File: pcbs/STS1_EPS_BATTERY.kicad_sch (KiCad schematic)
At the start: 10 parts, among them J3 Battery Pack, U13 TMCS1101A3B-Q1, U4 BQ29209DRBT

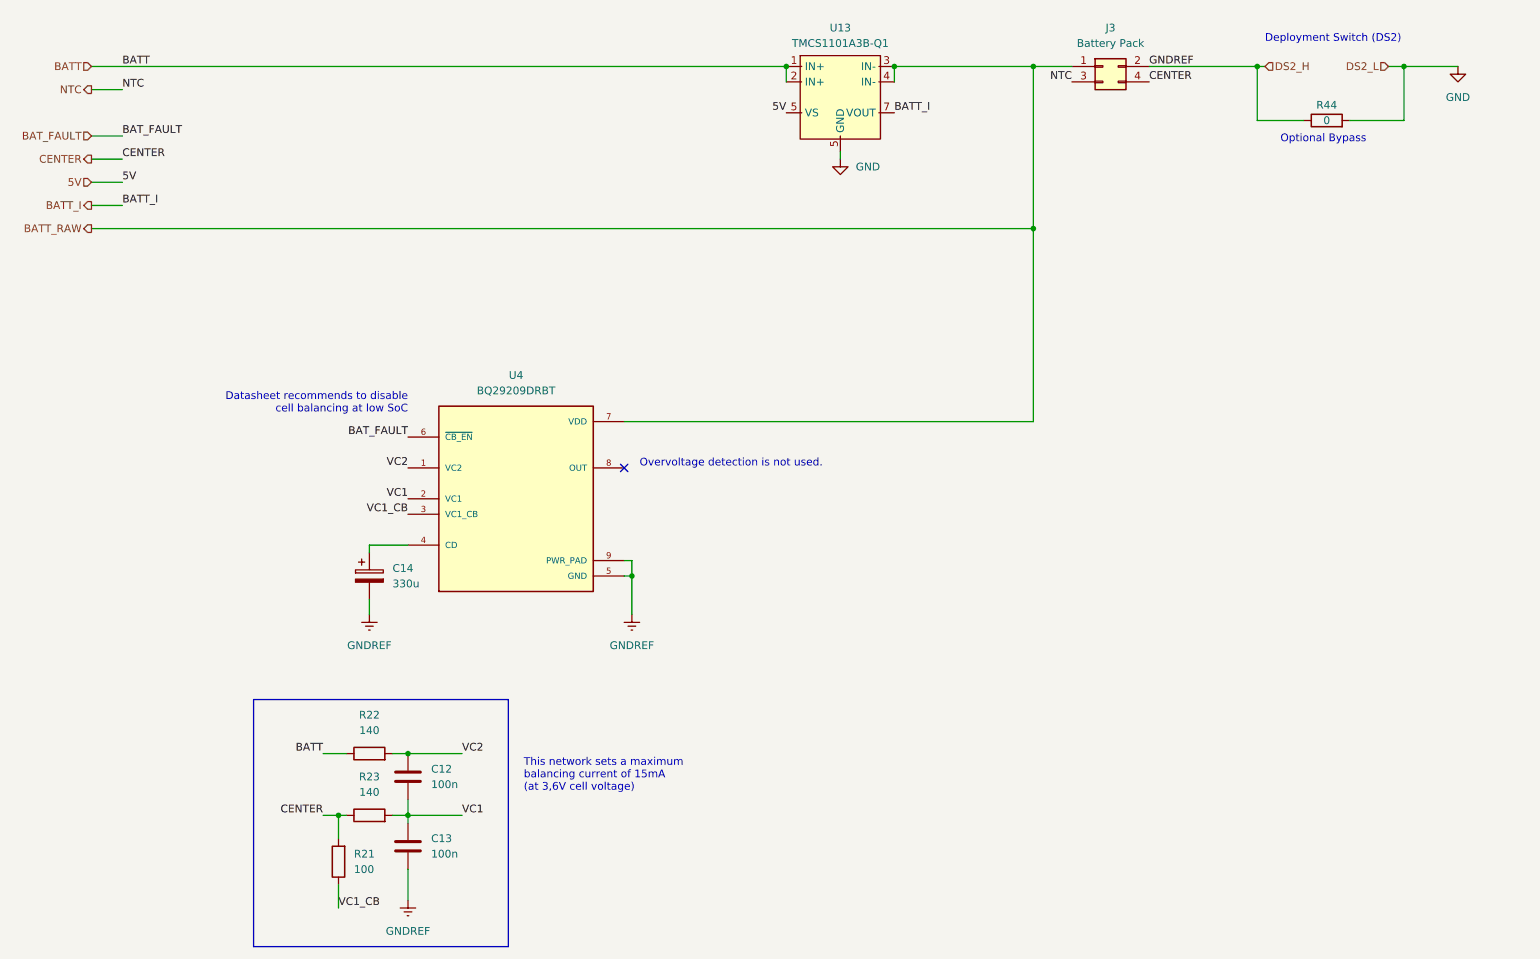
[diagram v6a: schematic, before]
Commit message: Worked on STS1_EPS_2 layout.
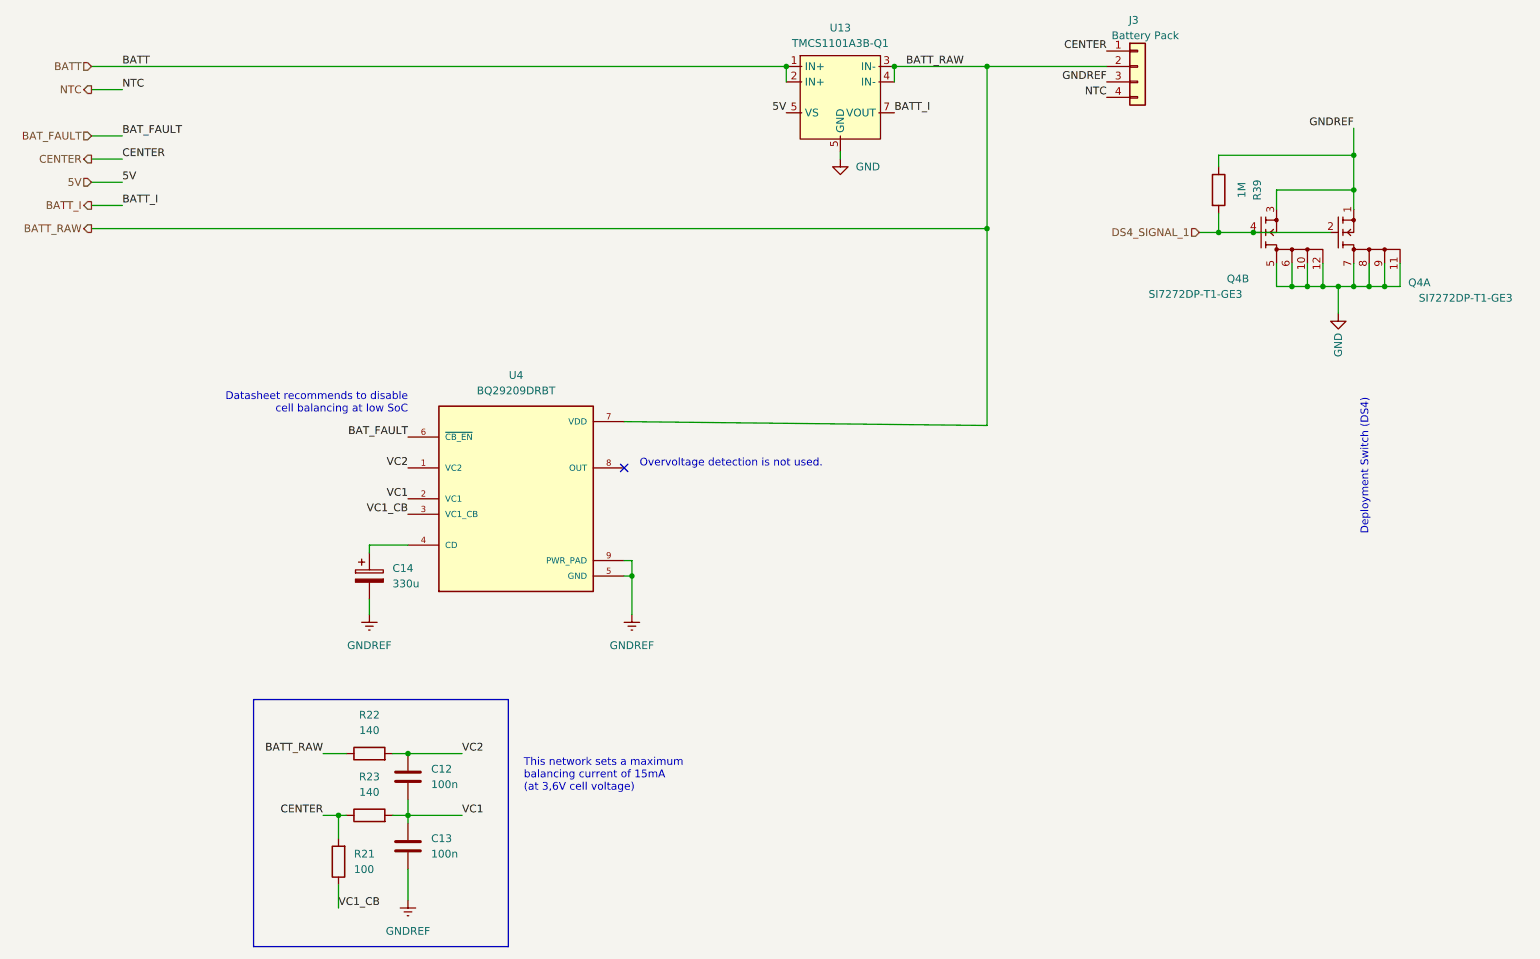
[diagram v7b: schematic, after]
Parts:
- removed R44: 0, Resistor_SMD:R_0805_2012Metric, symbol Device:R
- added Q4: SI7272DP-T1-GE3, STS_Package_SO:POWERPAK_SO8, symbol STS_Transistor_FET:SI7272DP-T1-GE3
- added R39: 1M, Resistor_SMD:R_0805_2012Metric, symbol Device:R
- J3: symbol Connector_Generic:Conn_02x02_Odd_Even -> Connector_Generic:Conn_01x04
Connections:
- net BATT: no longer R22.1
- net BATT_RAW: now also J3.2 (Pin_2), R22.1; no longer J3.1 (Pin_1)
- net CENTER: now also J3.1 (Pin_1); no longer J3.4 (Pin_4)
- net GND: now also Q4.10 (D2_3), Q4.11 (D1_4), Q4.12 (D2_4), Q4.5 (D2_1), Q4.6 (D2_2), Q4.7 (D1_1), Q4.8 (D1_2), Q4.9 (D1_3)
- net GNDREF: now also J3.3 (Pin_3), Q4.1 (S1), Q4.3 (S2), R39.1; no longer J3.2 (Pin_2)
- net NTC: now also J3.4 (Pin_4); no longer J3.3 (Pin_3)
- new net DS4_SIGNAL_1: Q4.2 (G1), Q4.4 (G2), R39.2
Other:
- note added: "Deployment Switch (DS4)"
- note removed: "Deployment Switch (DS2)"
- note removed: "Optional Bypass"
- moved on the sheet: J3
